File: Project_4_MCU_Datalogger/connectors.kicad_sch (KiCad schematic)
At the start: 4 parts, among them J1 Conn_01x04_Pin

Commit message: project 4 symbols arranged
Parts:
- gave numbers to parts that had none: 3
- renumbered J1 to J3
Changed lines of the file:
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@@
 		(on_board yes)
 		(dnp no)
-		(property "Reference" "J?"
+		(property "Reference" "J4"
 			(at 139.7 57.15 0)
 			(effects
@@
 			(project ""
 				(path "/4c892bc0-4cec-49d8-a0c6-54993ea1bf94/1975ca90-a7b1-42e7-a59a-5054cc7640fc"
-					(reference "J?")
+					(reference "J4")
 					(unit 1)
 				)
@@
 		(on_board yes)
 		(dnp no)
-		(property "Reference" "J?"
+		(property "Reference" "J2"
 			(at 109.855 58.42 0)
 			(effects
@@
 			(project ""
 				(path "/4c892bc0-4cec-49d8-a0c6-54993ea1bf94/1975ca90-a7b1-42e7-a59a-5054cc7640fc"
-					(reference "J?")
+					(reference "J2")
 					(unit 1)
 				)
@@
 		(on_board yes)
 		(dnp no)
-		(property "Reference" "J1"
+		(property "Reference" "J3"
 			(at 135.255 33.02 0)
 			(effects
@@
 			(project "Project_4_MCU_Datalogger"
 				(path "/4c892bc0-4cec-49d8-a0c6-54993ea1bf94/1975ca90-a7b1-42e7-a59a-5054cc7640fc"
-					(reference "J1")
+					(reference "J3")
 					(unit 1)
 				)
@@
 		(on_board yes)
 		(dnp no)
-		(property "Reference" "J?"
+		(property "Reference" "J1"
 			(at 108.585 33.02 0)
 			(effects
@@
 			(project ""
 				(path "/4c892bc0-4cec-49d8-a0c6-54993ea1bf94/1975ca90-a7b1-42e7-a59a-5054cc7640fc"
-					(reference "J?")
+					(reference "J1")
 					(unit 1)
 				)

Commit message: project 4 completed symbol-footprint associations
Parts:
- J1, J3: footprint (none) -> Connector_PinHeader_2.54mm:PinHeader_1x04_P2.54mm_Vertical
- J2: footprint (none) -> Connector_PinHeader_2.54mm:PinHeader_1x09_P2.54mm_Vertical
- J4: footprint (none) -> Connector_PinHeader_2.54mm:PinHeader_2x03_P2.54mm_Vertical
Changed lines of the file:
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@@
 			)
 		)
-		(property "Footprint" ""
+		(property "Footprint" "Connector_PinHeader_2.54mm:PinHeader_2x03_P2.54mm_Vertical"
 			(at 138.43 66.04 0)
 			(effects
@@
 			)
 		)
-		(property "Footprint" ""
+		(property "Footprint" "Connector_PinHeader_2.54mm:PinHeader_1x09_P2.54mm_Vertical"
 			(at 109.22 73.66 0)
 			(effects
@@
 			)
 		)
-		(property "Footprint" ""
+		(property "Footprint" "Connector_PinHeader_2.54mm:PinHeader_1x04_P2.54mm_Vertical"
 			(at 134.62 40.64 0)
 			(effects
@@
 			)
 		)
-		(property "Footprint" ""
+		(property "Footprint" "Connector_PinHeader_2.54mm:PinHeader_1x04_P2.54mm_Vertical"
 			(at 107.95 40.64 0)
 			(effects

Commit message: completed wiring
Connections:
- net MISO: now reaches J4.1 (Pin_1)
- net VCC: now reaches J4.2 (Pin_2)
- net VCC: now also J1.2 (Pin_2), J2.9 (Pin_9), J3.2 (Pin_2)
- net SCLK: now reaches J4.3 (Pin_3)
- net MOSI: now reaches J4.4 (Pin_4)
- net RESET: now reaches J4.5 (Pin_5)
- net GND: now reaches J4.6 (Pin_6)
- net GND: now also J1.1 (Pin_1), J2.8 (Pin_8), J3.1 (Pin_1)
- net D2: now reaches J2.1 (Pin_1)
- net D3: now reaches J2.2 (Pin_2)
- net D4: now reaches J2.3 (Pin_3)
- net D5: now reaches J2.4 (Pin_4)
- net D6: now reaches J2.5 (Pin_5)
- net D7: now reaches J2.6 (Pin_6)
- net D8: now reaches J2.7 (Pin_7)
- net RX: now reaches J3.3 (Pin_3)
- net TX: now reaches J3.4 (Pin_4)
- net SDA: now reaches J1.3 (Pin_3)
- net SCL: now reaches J1.4 (Pin_4)
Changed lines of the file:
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@@
 		(company "${author}")
+	)
+	(hierarchical_label "VCC"
+		(shape passive)
+		(at 139.7 40.64 0)
+		(effects
+			(font
+				(size 1.27 1.27)
+			)
+			(justify left)
+		)
+	)
+	(hierarchical_label "RX"
+		(shape input)
+		(at 139.7 43.18 0)
+		(effects
+			(font
+				(size 1.27 1.27)
+			)
+			(justify left)
+		)
+	)
+	(hierarchical_label "D7"
+		(shape bidirectional)
+		(at 114.3 76.2 0)
+		(effects
+			(font
+				(size 1.27 1.27)
+			)
+			(justify left)
+		)
+	)
+	(hierarchical_label "GND"
+		(shape passive)
+		(at 139.7 38.1 0)
+		(effects
+			(font
+				(size 1.27 1.27)
+			)
+			(justify left)
+		)
+	)
+	(hierarchical_label "RESET"
+		(shape passive)
+		(at 133.35 68.58 180)
+		(effects
+			(font
+				(size 1.27 1.27)
+			)
+			(justify right)
+		)
+	)
+	(hierarchical_label "TX"
+		(shape output)
+		(at 139.7 45.72 0)
+		(effects
+			(font
+				(size 1.27 1.27)
+			)
+			(justify left)
+		)
+	)
+	(hierarchical_label "GND"
+		(shape passive)
+		(at 113.03 38.1 0)
+		(effects
+			(font
+				(size 1.27 1.27)
+			)
+			(justify left)
+		)
+	)
+	(hierarchical_label "D5"
+		(shape bidirectional)
+		(at 114.3 71.12 0)
+		(effects
+			(font
+				(size 1.27 1.27)
+			)
+			(justify left)
+		)
+	)
+	(hierarchical_label "GND"
+		(shape passive)
+		(at 114.3 81.28 0)
+		(effects
+			(font
+				(size 1.27 1.27)
+			)
+			(justify left)
+		)
+	)
+	(hierarchical_label "D8"
+		(shape bidirectional)
+		(at 114.3 78.74 0)
+		(effects
+			(font
+				(size 1.27 1.27)
+			)
+			(justify left)
+		)
+	)
+	(hierarchical_label "MOSI"
+		(shape input)
+		(at 146.05 66.04 0)
+		(effects
+			(font
+				(size 1.27 1.27)
+			)
+			(justify left)
+		)
+	)
+	(hierarchical_label "MISO"
+		(shape output)
+		(at 133.35 63.5 180)
+		(effects
+			(font
+				(size 1.27 1.27)
+			)
+			(justify right)
+		)
+	)
+	(hierarchical_label "D6"
+		(shape bidirectional)
+		(at 114.3 73.66 0)
+		(effects
+			(font
+				(size 1.27 1.27)
+			)
+			(justify left)
+		)
+	)
+	(hierarchical_label "D3"
+		(shape bidirectional)
+		(at 114.3 66.04 0)
+		(effects
+			(font
+				(size 1.27 1.27)
+			)
+			(justify left)
+		)
+	)
+	(hierarchical_label "VCC"
+		(shape passive)
+		(at 146.05 63.5 0)
+		(effects
+			(font
+				(size 1.27 1.27)
+			)
+			(justify left)
+		)
+	)
+	(hierarchical_label "GND"
+		(shape passive)
+		(at 146.05 68.58 0)
+		(effects
+			(font
+				(size 1.27 1.27)
+			)
+			(justify left)
+		)
+	)
+	(hierarchical_label "SCLK"
+		(shape passive)
+		(at 133.35 66.04 180)
+		(effects
+			(font
+				(size 1.27 1.27)
+			)
+			(justify right)
+		)
+	)
+	(hierarchical_label "SCL"
+		(shape passive)
+		(at 113.03 45.72 0)
+		(effects
+			(font
+				(size 1.27 1.27)
+			)
+			(justify left)
+		)
+	)
+	(hierarchical_label "VCC"
+		(shape passive)
+		(at 114.3 83.82 0)
+		(effects
+			(font
+				(size 1.27 1.27)
+			)
+			(justify left)
+		)
+	)
+	(hierarchical_label "D4"
+		(shape bidirectional)
+		(at 114.3 68.58 0)
+		(effects
+			(font
+				(size 1.27 1.27)
+			)
+			(justify left)
+		)
+	)
+	(hierarchical_label "D2"
+		(shape bidirectional)
+		(at 114.3 63.5 0)
+		(effects
+			(font
+				(size 1.27 1.27)
+			)
+			(justify left)
+		)
+	)
+	(hierarchical_label "VCC"
+		(shape passive)
+		(at 113.03 40.64 0)
+		(effects
+			(font
+				(size 1.27 1.27)
+			)
+			(justify left)
+		)
+	)
+	(hierarchical_label "SDA"
+		(shape bidirectional)
+		(at 113.03 43.18 0)
+		(effects
+			(font
+				(size 1.27 1.27)
+			)
+			(justify left)
+		)
 	)
 	(symbol

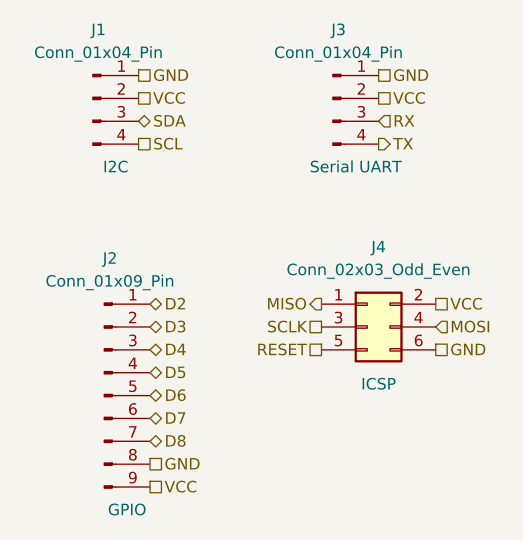
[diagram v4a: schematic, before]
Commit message: schematic completed
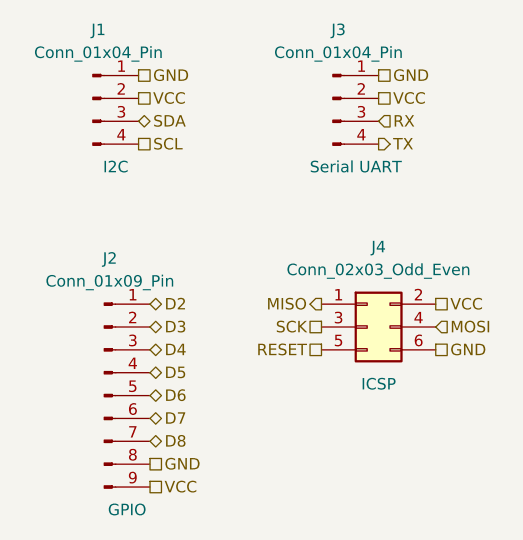
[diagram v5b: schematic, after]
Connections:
- net SCLK renamed SCK
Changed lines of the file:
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@@
 		)
 	)
-	(hierarchical_label "SCLK"
+	(hierarchical_label "SCK"
 		(shape passive)
 		(at 133.35 66.04 180)
